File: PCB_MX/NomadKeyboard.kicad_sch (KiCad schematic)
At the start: 91 parts, among them J1 4PIN, J2 OLED, SW1 SW_PUSH_LED, SW10 SW_PUSH_LED, SW11 SW_PUSH_LED, SW12 SW_PUSH_LED, SW13 SW_PUSH_LED, SW14 SW_PUSH_LED, SW15 SW_PUSH_LED, SW16 SW_PUSH_LED, SW17 SW_PUSH_LED, SW18 SW_PUSH_LED, SW19 SW_PUSH_LED, SW2 SW_PUSH_LED, SW20 SW_PUSH_LED, SW21 SW_PUSH_LED, SW22 SW_PUSH_LED, SW23 SW_PUSH_LED, SW24 SW_PUSH_LED, SW25 SW_PUSH_LED, SW26 SW_PUSH_LED, SW27 SW_PUSH_LED, SW28 SW_PUSH_LED, SW29 SW_PUSH_LED, SW3 SW_PUSH_LED, SW30 SW_PUSH_LED, SW31 SW_PUSH_LED, SW32 SW_PUSH_LED, SW33 SW_PUSH_LED, SW34 SW_PUSH_LED, SW4 SW_PUSH_LED, SW5 SW_PUSH_LED, SW6 SW_PUSH_LED, SW7 SW_PUSH_LED, SW8 SW_PUSH_LED, SW9 SW_PUSH_LED, U1 ProMicro

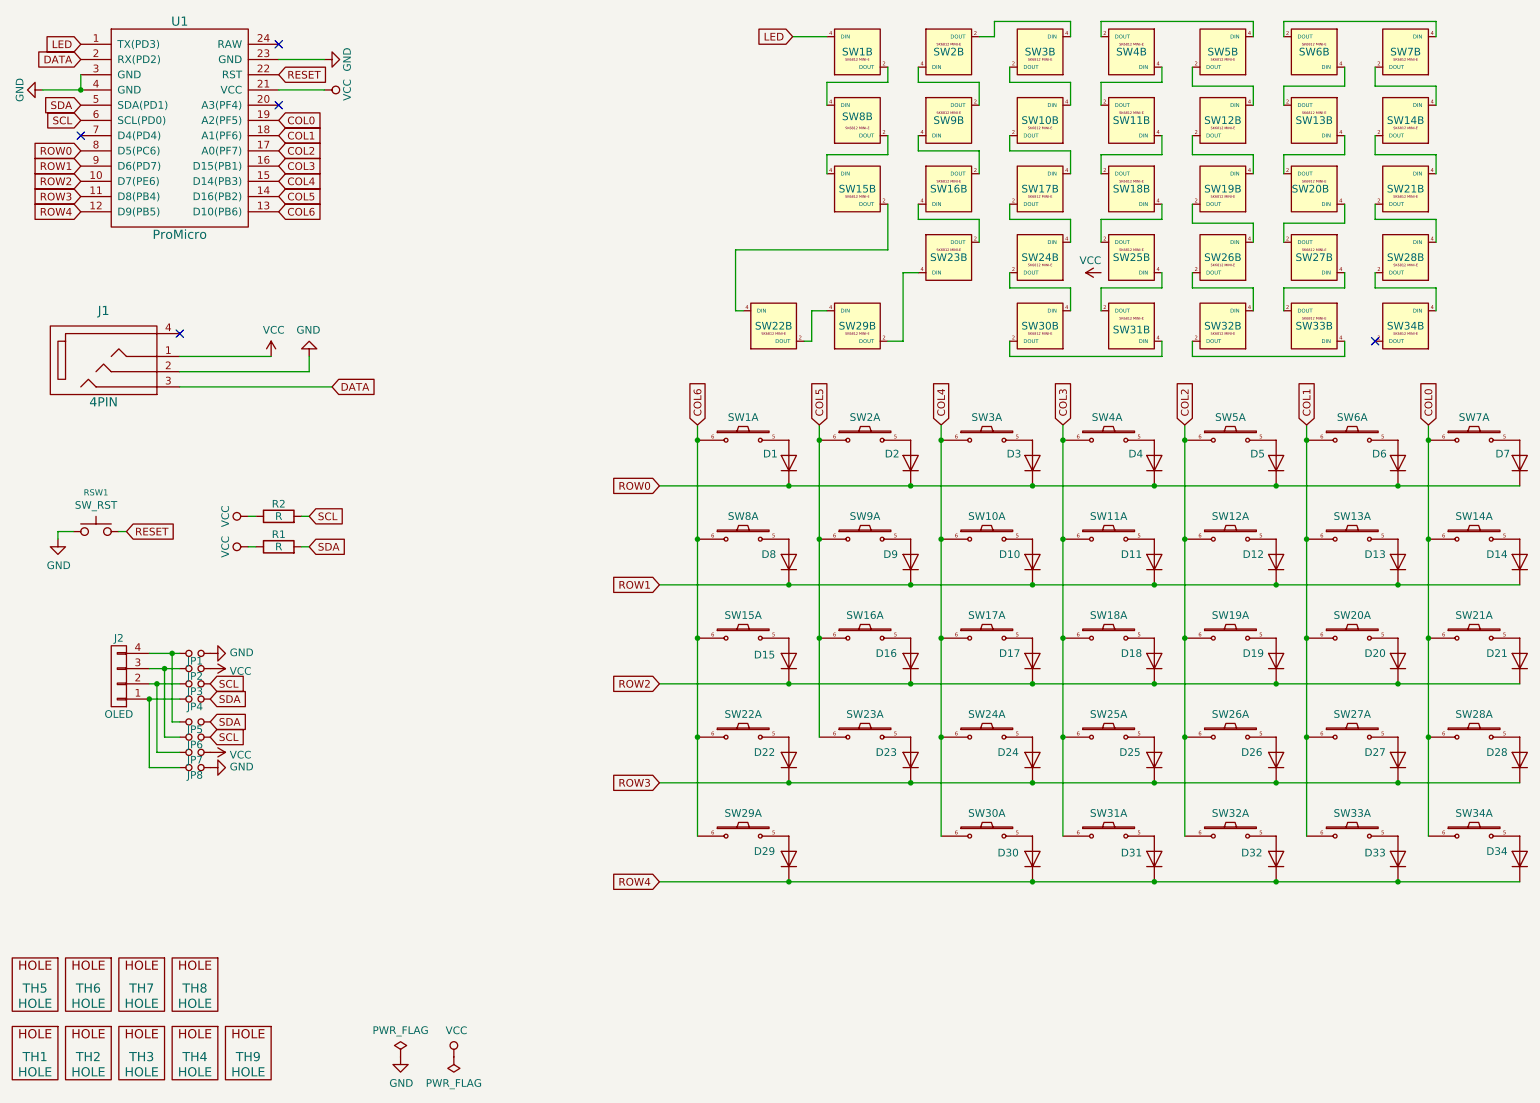
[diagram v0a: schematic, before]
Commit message: Nomad Rev 2
* Exclusively supports RP2040 CE microcontrollers
* Only one set of headers for hte RP2040 with solder jumpers to select
  the half
* EC12 low-profile rotary encoder support
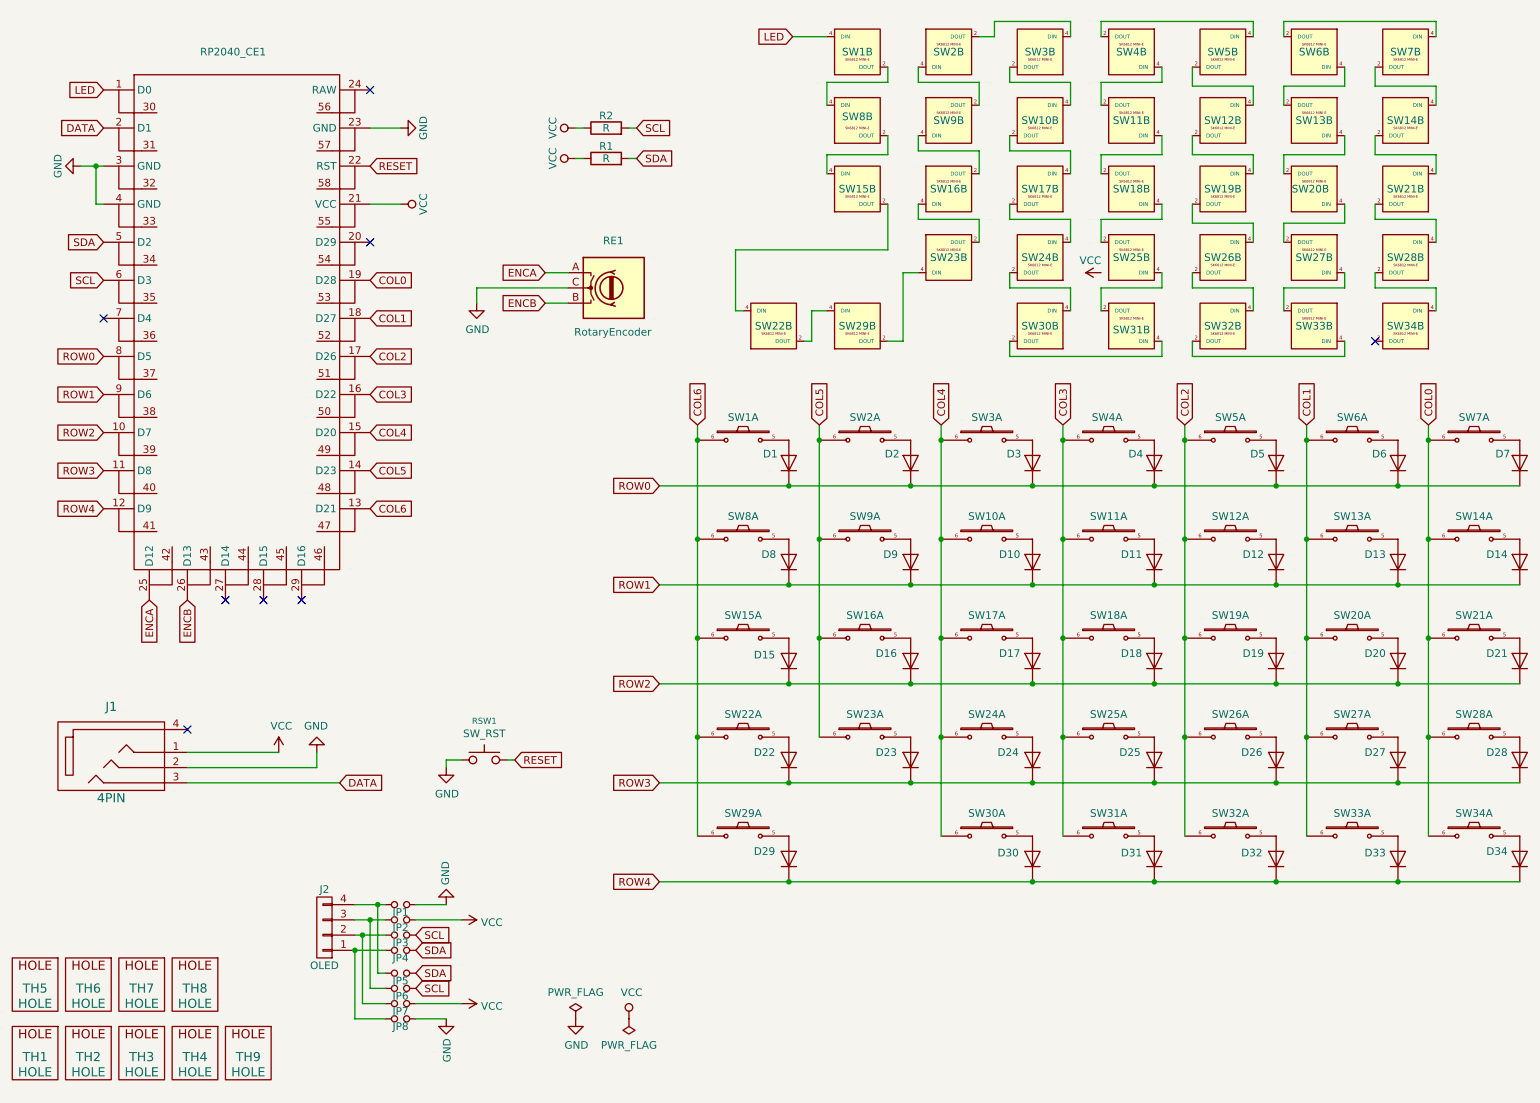
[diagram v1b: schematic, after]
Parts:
- removed U1: ProMicro, SofleChoc:ProMicro, symbol SofleKeyboard-rescue:ProMicro_2-Lily58-cache-Lily58_Pro-rescue
- added RE1: RotaryEncoder, Rotary_Encoder:RotaryEncoder_Alps_EC12E_Vertical_H20mm, symbol Device:RotaryEncoder
- added RP2040_CE1: ~, Nomad:RP2040_CE, symbol Nomad:RP2040_CE
- R1, R2: footprint SofleChoc:RESISTOR_mini -> Nomad:R_1206_3216Metric_Pad1.30x1.75mm_HandSolder
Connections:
- net COL0: now also RP2040_CE1.19 (D28)
- net COL1: now also RP2040_CE1.18 (D27)
- net COL2: now also RP2040_CE1.17 (D26)
- net COL3: now also RP2040_CE1.16 (D22)
- net COL4: now also RP2040_CE1.15 (D20)
- net COL5: now also RP2040_CE1.14 (D23)
- net COL6: now also RP2040_CE1.13 (D21)
- net DATA: now also RP2040_CE1.2 (D1)
- net GND: now also RE1.C, RP2040_CE1.23 (GND), RP2040_CE1.3 (GND), RP2040_CE1.4 (GND)
- net LED: now also RP2040_CE1.1 (D0)
- net RESET: now also RP2040_CE1.22 (RST)
- net ROW0: now also RP2040_CE1.8 (D5)
- net ROW1: now also RP2040_CE1.9 (D6)
- net ROW2: now also RP2040_CE1.10 (D7)
- net ROW3: now also RP2040_CE1.11 (D8)
- net ROW4: now also RP2040_CE1.12 (D9)
- net SCL: now also RP2040_CE1.6 (D3)
- net SDA: now also RP2040_CE1.5 (D2)
- net VCC: now also RP2040_CE1.21 (VCC)
- new net ENCA: RE1.A, RP2040_CE1.25 (D12)
- new net ENCB: RE1.B, RP2040_CE1.26 (D13)
- no-connect marks 5 -> 8
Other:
- moved on the sheet: J1, J2, JP1, JP2, JP3, JP4, JP5, JP6, JP7, JP8, R1, R2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
